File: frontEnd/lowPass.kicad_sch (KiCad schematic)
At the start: 15 parts, among them U201 BGS12P2L6E6327XTSA1, U202 BGS12P2L6E6327XTSA1

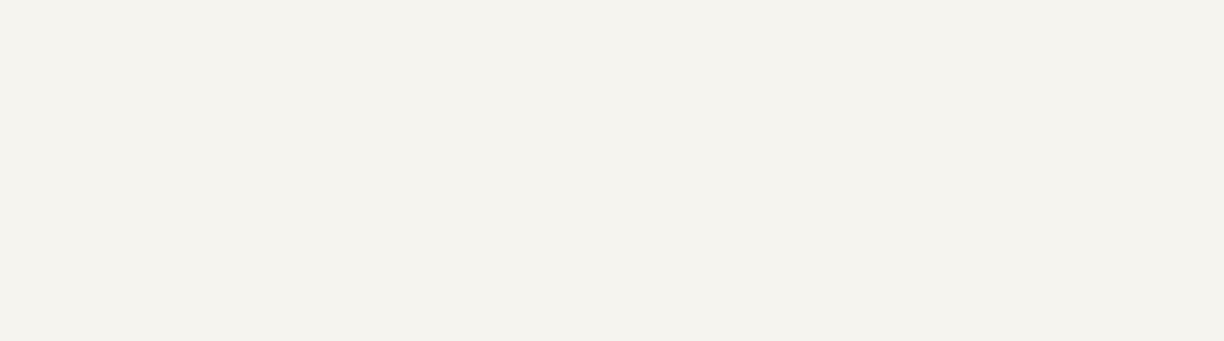
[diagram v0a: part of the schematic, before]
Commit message: update schematics, add bypass for the attenuator
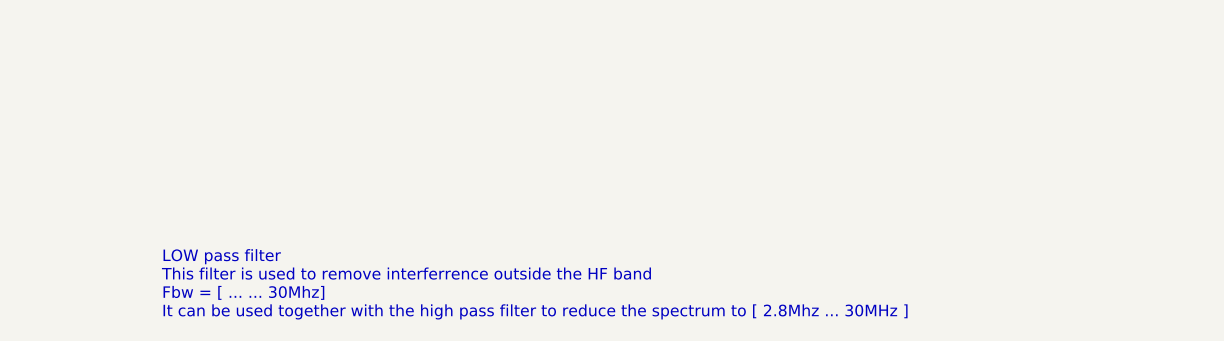
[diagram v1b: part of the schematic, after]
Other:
- note added: "LOW pass filter This filter is used to remove interferrence outside the HF band Fbw = [ ... ... 30Mhz] It can be used together with the high pass filter to reduce the spectrum to [ 2.8Mhz ... 30MHz ]"
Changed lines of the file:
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@@
     (stroke (width 0) (type default) (color 0 0 0 0))
+  )
+  (text "LOW pass filter\nThis filter is used to remove interferrence outside the HF band\nFbw = [ ... ... 30Mhz]\nIt can be used together with the high pass filter to reduce the spectrum to [ 2.8Mhz ... 30MHz ]"
+    (at 179.07 177.8 0)
+    (effects (font (size 1.27 1.27)) (justify left bottom))
   )
   (hierarchical_label "RF_IN" (shape input) (at 41.91 78.74 180)

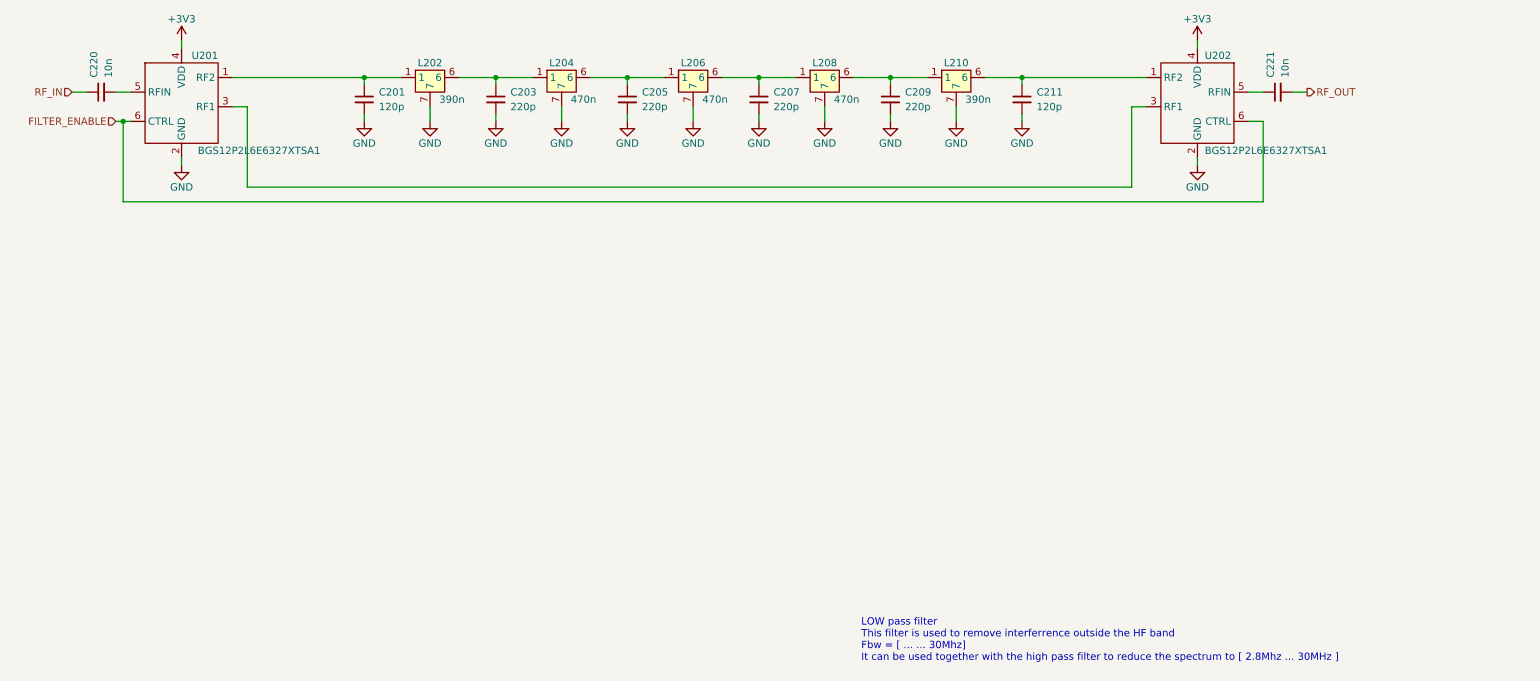
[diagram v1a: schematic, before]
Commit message: simply schematic: remove attenuator and gain blocks; add 5 way multiplexer
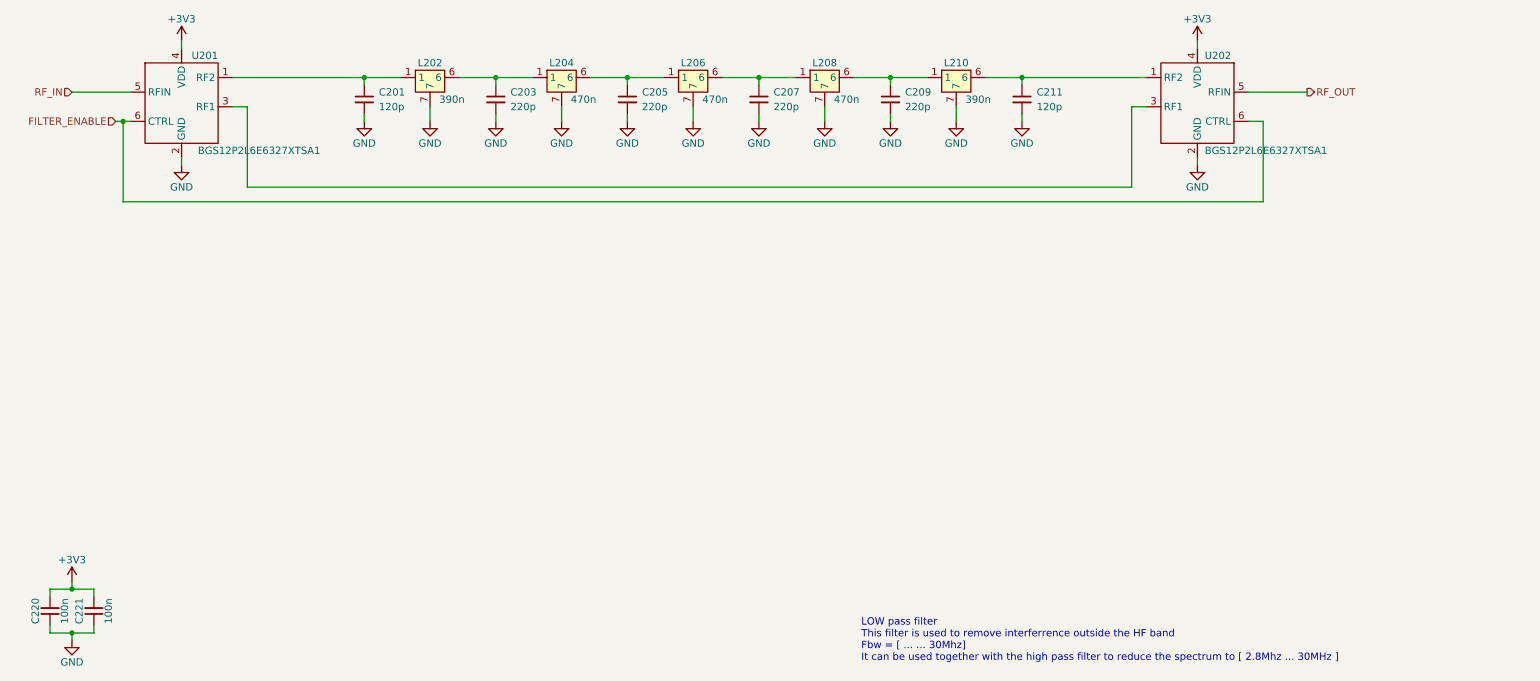
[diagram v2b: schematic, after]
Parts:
- C220, C221: value 10n -> 100n
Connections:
- net +3V3: now also C220.2, C221.2
- net GND: now also C220.1, C221.1
- net RF_IN: now also U201.5 (RFIN); no longer C220.1
- net RF_OUT: now also U202.5 (RFIN); no longer C221.2
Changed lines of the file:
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@@
   (junction (at 161.29 76.2) (diameter 0) (color 0 0 0 0)
   )
+  (junction (at 41.91 165.1) (diameter 0) (color 0 0 0 0)
+  )
   (junction (at 115.57 76.2) (diameter 0) (color 0 0 0 0)
   )
   (junction (at 207.01 76.2) (diameter 0) (color 0 0 0 0)
   )
+  (junction (at 41.91 172.72) (diameter 0) (color 0 0 0 0)
+  )
   (junction (at 184.15 76.2) (diameter 0) (color 0 0 0 0)
   )
@@
     (stroke (width 0) (type default) (color 0 0 0 0))
   )
+  (wire (pts (xy 41.91 172.72) (xy 41.91 173.99))
+    (stroke (width 0) (type default) (color 0 0 0 0))
+  )
   (wire (pts (xy 161.29 76.2) (xy 167.64 76.2))
     (stroke (width 0) (type default) (color 0 0 0 0))
@@
     (stroke (width 0) (type default) (color 0 0 0 0))
   )
+  (wire (pts (xy 41.91 172.72) (xy 45.72 172.72))
+    (stroke (width 0) (type default) (color 0 0 0 0))
+  )
   (wire (pts (xy 154.94 76.2) (xy 161.29 76.2))
     (stroke (width 0) (type default) (color 0 0 0 0))
@@
     (stroke (width 0) (type default) (color 0 0 0 0))
   )
-  (wire (pts (xy 41.91 78.74) (xy 44.45 78.74))
-    (stroke (width 0) (type default) (color 0 0 0 0))
-  )
   (wire (pts (xy 69.85 81.28) (xy 72.39 81.28))
     (stroke (width 0) (type default) (color 0 0 0 0))
@@
     (stroke (width 0) (type default) (color 0 0 0 0))
   )
-  (wire (pts (xy 254 78.74) (xy 256.54 78.74))
+  (wire (pts (xy 38.1 172.72) (xy 41.91 172.72))
     (stroke (width 0) (type default) (color 0 0 0 0))
   )
@@
     (stroke (width 0) (type default) (color 0 0 0 0))
   )
+  (wire (pts (xy 41.91 165.1) (xy 45.72 165.1))
+    (stroke (width 0) (type default) (color 0 0 0 0))
+  )
   (wire (pts (xy 127 81.28) (xy 127 83.82))
     (stroke (width 0) (type default) (color 0 0 0 0))
@@
     (stroke (width 0) (type default) (color 0 0 0 0))
   )
+  (wire (pts (xy 38.1 166.37) (xy 38.1 165.1))
+    (stroke (width 0) (type default) (color 0 0 0 0))
+  )
+  (wire (pts (xy 45.72 165.1) (xy 45.72 166.37))
+    (stroke (width 0) (type default) (color 0 0 0 0))
+  )
   (wire (pts (xy 226.06 81.28) (xy 226.06 95.25))
     (stroke (width 0) (type default) (color 0 0 0 0))
@@
     (stroke (width 0) (type default) (color 0 0 0 0))
   )
-  (wire (pts (xy 49.53 78.74) (xy 52.07 78.74))
+  (wire (pts (xy 38.1 165.1) (xy 41.91 165.1))
+    (stroke (width 0) (type default) (color 0 0 0 0))
+  )
+  (wire (pts (xy 38.1 171.45) (xy 38.1 172.72))
+    (stroke (width 0) (type default) (color 0 0 0 0))
+  )
+  (wire (pts (xy 41.91 78.74) (xy 52.07 78.74))
     (stroke (width 0) (type default) (color 0 0 0 0))
   )
@@
     (stroke (width 0) (type default) (color 0 0 0 0))
   )
+  (wire (pts (xy 45.72 171.45) (xy 45.72 172.72))
+    (stroke (width 0) (type default) (color 0 0 0 0))
+  )
   (wire (pts (xy 207.01 76.2) (xy 207.01 77.47))
     (stroke (width 0) (type default) (color 0 0 0 0))
@@
     (stroke (width 0) (type default) (color 0 0 0 0))
   )
-  (wire (pts (xy 246.38 78.74) (xy 248.92 78.74))
+  (wire (pts (xy 246.38 78.74) (xy 256.54 78.74))
+    (stroke (width 0) (type default) (color 0 0 0 0))
+  )
+  (wire (pts (xy 41.91 163.83) (xy 41.91 165.1))
     (stroke (width 0) (type default) (color 0 0 0 0))
   )
@@
     (effects (font (size 1.27 1.27)) (justify left))
   )
-  (symbol (lib_id "Device:C_Small") (at 46.99 78.74 90) (unit 1)
-    (in_bom yes) (on_board yes)
-    (property "Reference" "C220" (id 0) (at 45.7262 76.2 0)
-      (effects (font (size 1.27 1.27)) (justify left))
-    )
-    (property "Value" "10n" (id 1) (at 48.2662 76.2 0)
-      (effects (font (size 1.27 1.27)) (justify left))
-    )
-    (property "Footprint" "Capacitor_SMD:C_0805_2012Metric" (id 2) (at 46.99 78.74 0)
-      (effects (font (size 1.27 1.27)) hide)
-    )
-    (property "Datasheet" "~" (id 3) (at 46.99 78.74 0)
+  (symbol (lib_id "Device:C_Small") (at 45.72 168.91 180) (unit 1)
+    (in_bom yes) (on_board yes)
+    (property "Reference" "C221" (id 0) (at 43.18 168.91 90))
+    (property "Value" "100n" (id 1) (at 48.26 168.91 90))
+    (property "Footprint" "Capacitor_SMD:C_0805_2012Metric" (id 2) (at 45.72 168.91 0)
+      (effects (font (size 1.27 1.27)) hide)
+    )
+    (property "Datasheet" "~" (id 3) (at 45.72 168.91 0)
       (effects (font (size 1.27 1.27)) hide)
     )
@@
     (pin "2")
   )
-  (symbol (lib_id "Device:C_Small") (at 251.46 78.74 90) (unit 1)
-    (in_bom yes) (on_board yes)
-    (property "Reference" "C221" (id 0) (at 250.1962 76.2 0)
-      (effects (font (size 1.27 1.27)) (justify left))
-    )
-    (property "Value" "10n" (id 1) (at 252.7362 76.2 0)
-      (effects (font (size 1.27 1.27)) (justify left))
-    )
-    (property "Footprint" "Capacitor_SMD:C_0805_2012Metric" (id 2) (at 251.46 78.74 0)
-      (effects (font (size 1.27 1.27)) hide)
-    )
-    (property "Datasheet" "~" (id 3) (at 251.46 78.74 0)
+  (symbol (lib_id "power:+3V3") (at 41.91 163.83 0) (unit 1)
+    (in_bom yes) (on_board yes)
+    (property "Reference" "#PWR?" (id 0) (at 41.91 167.64 0)
+      (effects (font (size 1.27 1.27)) hide)
+    )
+    (property "Value" "+3V3" (id 1) (at 41.91 160.02 0))
+    (property "Footprint" "" (id 2) (at 41.91 163.83 0)
+      (effects (font (size 1.27 1.27)) hide)
+    )
+    (property "Datasheet" "" (id 3) (at 41.91 163.83 0)
+      (effects (font (size 1.27 1.27)) hide)
+    )
+    (pin "1")
+  )
+  (symbol (lib_id "Device:C_Small") (at 38.1 168.91 180) (unit 1)
+    (in_bom yes) (on_board yes)
+    (property "Reference" "C220" (id 0) (at 35.56 168.91 90))
+    (property "Value" "100n" (id 1) (at 40.64 168.91 90))
+    (property "Footprint" "Capacitor_SMD:C_0805_2012Metric" (id 2) (at 38.1 168.91 0)
+      (effects (font (size 1.27 1.27)) hide)
+    )
+    (property "Datasheet" "~" (id 3) (at 38.1 168.91 0)
       (effects (font (size 1.27 1.27)) hide)
     )
@@
     (pin "2")
   )
+  (symbol (lib_id "power:GND") (at 41.91 173.99 0) (unit 1)
+    (in_bom yes) (on_board yes)
+    (property "Reference" "#PWR?" (id 0) (at 41.91 180.34 0)
+      (effects (font (size 1.27 1.27)) hide)
+    )
+    (property "Value" "GND" (id 1) (at 41.91 177.8 0))
+    (property "Footprint" "" (id 2) (at 41.91 173.99 0)
+      (effects (font (size 1.27 1.27)) hide)
+    )
+    (property "Datasheet" "" (id 3) (at 41.91 173.99 0)
+      (effects (font (size 1.27 1.27)) hide)
+    )
+    (pin "1")
+  )
   (symbol (lib_id "Device:C_Small") (at 138.43 80.01 0) (unit 1)

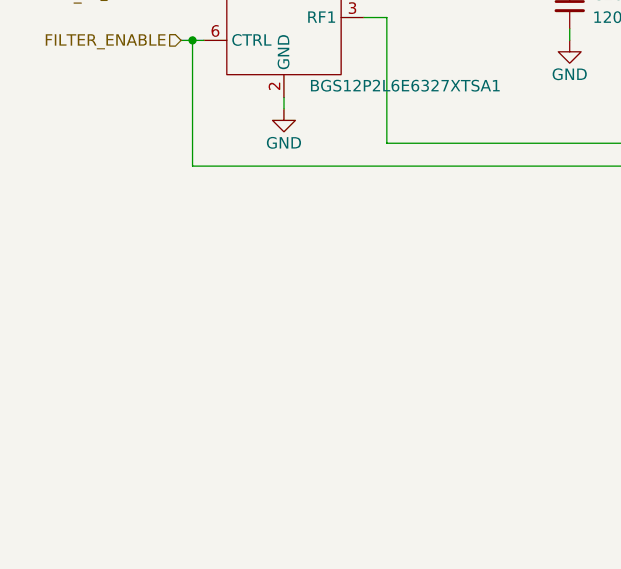
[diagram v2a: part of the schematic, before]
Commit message: add leds for each filter block
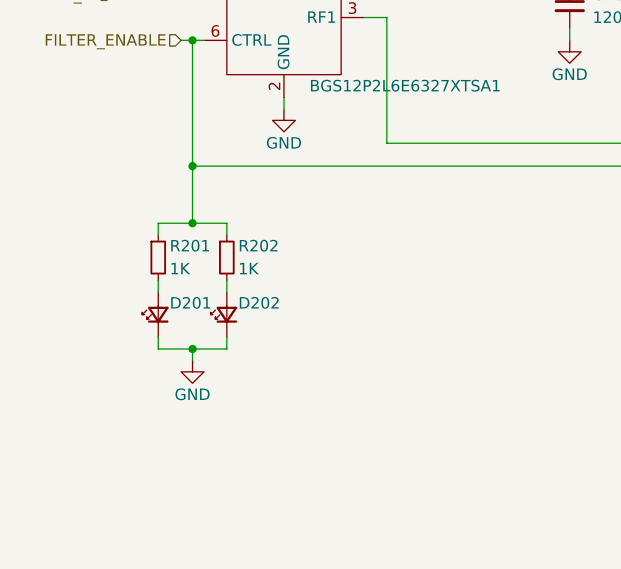
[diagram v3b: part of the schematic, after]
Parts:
- added D201, D202: LED_Small, LED_SMD:LED_0805_2012Metric, symbol Device:LED_Small
- added R201, R202: 1K, Resistor_SMD:R_0805_2012Metric, symbol Device:R_Small
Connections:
- net FILTER_ENABLE: now also R201.1, R202.1
- net GND: now also D201.1 (K), D202.1 (K)
- new net: D201.2 (A), R201.2
- new net: D202.2 (A), R202.2
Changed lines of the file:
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@@
   (junction (at 138.43 76.2) (diameter 0) (color 0 0 0 0)
   )
+  (junction (at 50.8 97.79) (diameter 0) (color 0 0 0 0)
+  )
+  (junction (at 50.8 118.11) (diameter 0) (color 0 0 0 0)
+  )
+  (junction (at 50.8 104.14) (diameter 0) (color 0 0 0 0)
+  )
   (junction (at 50.8 83.82) (diameter 0) (color 0 0 0 0)
   )
@@
     (stroke (width 0) (type default) (color 0 0 0 0))
   )
+  (wire (pts (xy 50.8 118.11) (xy 50.8 119.38))
+    (stroke (width 0) (type default) (color 0 0 0 0))
+  )
   (wire (pts (xy 154.94 76.2) (xy 161.29 76.2))
     (stroke (width 0) (type default) (color 0 0 0 0))
@@
     (stroke (width 0) (type default) (color 0 0 0 0))
   )
+  (wire (pts (xy 50.8 104.14) (xy 54.61 104.14))
+    (stroke (width 0) (type default) (color 0 0 0 0))
+  )
   (wire (pts (xy 69.85 81.28) (xy 72.39 81.28))
     (stroke (width 0) (type default) (color 0 0 0 0))
@@
     (stroke (width 0) (type default) (color 0 0 0 0))
   )
+  (wire (pts (xy 54.61 104.14) (xy 54.61 105.41))
+    (stroke (width 0) (type default) (color 0 0 0 0))
+  )
   (wire (pts (xy 138.43 76.2) (xy 144.78 76.2))
     (stroke (width 0) (type default) (color 0 0 0 0))
@@
     (stroke (width 0) (type default) (color 0 0 0 0))
   )
+  (wire (pts (xy 46.99 110.49) (xy 46.99 111.76))
+    (stroke (width 0) (type default) (color 0 0 0 0))
+  )
   (wire (pts (xy 184.15 82.55) (xy 184.15 83.82))
     (stroke (width 0) (type default) (color 0 0 0 0))
@@
     (stroke (width 0) (type default) (color 0 0 0 0))
   )
+  (wire (pts (xy 46.99 116.84) (xy 46.99 118.11))
+    (stroke (width 0) (type default) (color 0 0 0 0))
+  )
   (wire (pts (xy 226.06 81.28) (xy 226.06 95.25))
     (stroke (width 0) (type default) (color 0 0 0 0))
@@
     (stroke (width 0) (type default) (color 0 0 0 0))
   )
+  (wire (pts (xy 46.99 105.41) (xy 46.99 104.14))
+    (stroke (width 0) (type default) (color 0 0 0 0))
+  )
+  (wire (pts (xy 54.61 110.49) (xy 54.61 111.76))
+    (stroke (width 0) (type default) (color 0 0 0 0))
+  )
   (wire (pts (xy 38.1 171.45) (xy 38.1 172.72))
     (stroke (width 0) (type default) (color 0 0 0 0))
@@
     (stroke (width 0) (type default) (color 0 0 0 0))
   )
+  (wire (pts (xy 54.61 116.84) (xy 54.61 118.11))
+    (stroke (width 0) (type default) (color 0 0 0 0))
+  )
   (wire (pts (xy 60.96 69.85) (xy 60.96 71.12))
     (stroke (width 0) (type default) (color 0 0 0 0))
@@
     (stroke (width 0) (type default) (color 0 0 0 0))
   )
+  (wire (pts (xy 50.8 97.79) (xy 50.8 104.14))
+    (stroke (width 0) (type default) (color 0 0 0 0))
+  )
+  (wire (pts (xy 46.99 118.11) (xy 50.8 118.11))
+    (stroke (width 0) (type default) (color 0 0 0 0))
+  )
   (wire (pts (xy 207.01 76.2) (xy 207.01 77.47))
     (stroke (width 0) (type default) (color 0 0 0 0))
@@
   )
   (wire (pts (xy 60.96 90.17) (xy 60.96 91.44))
+    (stroke (width 0) (type default) (color 0 0 0 0))
+  )
+  (wire (pts (xy 46.99 104.14) (xy 50.8 104.14))
+    (stroke (width 0) (type default) (color 0 0 0 0))
+  )
+  (wire (pts (xy 50.8 118.11) (xy 54.61 118.11))
     (stroke (width 0) (type default) (color 0 0 0 0))
   )
@@
     (pin "1")
   )
+  (symbol (lib_id "power:GND") (at 50.8 119.38 0) (unit 1)
+    (in_bom yes) (on_board yes)
+    (property "Reference" "#PWR?" (id 0) (at 50.8 125.73 0)
+      (effects (font (size 1.27 1.27)) hide)
+    )
+    (property "Value" "GND" (id 1) (at 50.8 123.19 0))
+    (property "Footprint" "" (id 2) (at 50.8 119.38 0)
+      (effects (font (size 1.27 1.27)) hide)
+    )
+    (property "Datasheet" "" (id 3) (at 50.8 119.38 0)
+      (effects (font (size 1.27 1.27)) hide)
+    )
+    (pin "1")
+  )
   (symbol (lib_id "Device:C_Small") (at 184.15 80.01 0) (unit 1)
     (in_bom yes) (on_board yes)
@@
     )
     (property "Datasheet" "~" (id 3) (at 184.15 80.01 0)
+      (effects (font (size 1.27 1.27)) hide)
+    )
+    (pin "1")
+    (pin "2")
+  )
+  (symbol (lib_id "Device:R_Small") (at 46.99 107.95 0) (unit 1)
+    (in_bom yes) (on_board yes)
+    (property "Reference" "R201" (id 0) (at 48.26 106.68 0)
+      (effects (font (size 1.27 1.27)) (justify left))
+    )
+    (property "Value" "1K" (id 1) (at 48.26 109.22 0)
+      (effects (font (size 1.27 1.27)) (justify left))
+    )
+    (property "Footprint" "Resistor_SMD:R_0805_2012Metric" (id 2) (at 46.99 107.95 0)
+      (effects (font (size 1.27 1.27)) hide)
+    )
+    (property "Datasheet" "~" (id 3) (at 46.99 107.95 0)
       (effects (font (size 1.27 1.27)) hide)
     )
@@
     (pin "1")
   )
+  (symbol (lib_id "Device:LED_Small") (at 54.61 114.3 90) (unit 1)
+    (in_bom yes) (on_board yes)
+    (property "Reference" "D202" (id 0) (at 55.88 113.03 90)
+      (effects (font (size 1.27 1.27)) (justify right))
+    )
+    (property "Value" "LED_Small" (id 1) (at 57.15 115.5064 90)
+      (effects (font (size 1.27 1.27)) (justify right) hide)
+    )
+    (property "Footprint" "LED_SMD:LED_0805_2012Metric" (id 2) (at 54.61 114.3 90)
+      (effects (font (size 1.27 1.27)) hide)
+    )
+    (property "Datasheet" "~" (id 3) (at 54.61 114.3 90)
+      (effects (font (size 1.27 1.27)) hide)
+    )
+    (pin "1")
+    (pin "2")
+  )
   (symbol (lib_id "frontEnd:TOKO_10K_SERIES") (at 193.04 76.2 0) (unit 1)
     (in_bom yes) (on_board yes)
@@
     (pin "2")
   )
+  (symbol (lib_id "Device:LED_Small") (at 46.99 114.3 90) (unit 1)
+    (in_bom yes) (on_board yes)
+    (property "Reference" "D201" (id 0) (at 48.26 113.03 90)
+      (effects (font (size 1.27 1.27)) (justify right))
+    )
+    (property "Value" "LED_Small" (id 1) (at 49.53 115.5064 90)
+      (effects (font (size 1.27 1.27)) (justify right) hide)
+    )
+    (property "Footprint" "LED_SMD:LED_0805_2012Metric" (id 2) (at 46.99 114.3 90)
+      (effects (font (size 1.27 1.27)) hide)
+    )
+    (property "Datasheet" "~" (id 3) (at 46.99 114.3 90)
+      (effects (font (size 1.27 1.27)) hide)
+    )
+    (pin "1")
+    (pin "2")
+  )
   (symbol (lib_id "power:GND") (at 237.49 91.44 0) (unit 1)
     (in_bom yes) (on_board yes)
@@
     (pin "1")
   )
+  (symbol (lib_id "Device:R_Small") (at 54.61 107.95 0) (unit 1)
+    (in_bom yes) (on_board yes)
+    (property "Reference" "R202" (id 0) (at 55.88 106.68 0)
+      (effects (font (size 1.27 1.27)) (justify left))
+    )
+    (property "Value" "1K" (id 1) (at 55.88 109.22 0)
+      (effects (font (size 1.27 1.27)) (justify left))
+    )
+    (property "Footprint" "Resistor_SMD:R_0805_2012Metric" (id 2) (at 54.61 107.95 0)
+      (effects (font (size 1.27 1.27)) hide)
+    )
+    (property "Datasheet" "~" (id 3) (at 54.61 107.95 0)
+      (effects (font (size 1.27 1.27)) hide)
+    )
+    (pin "1")
+    (pin "2")
+  )
   (symbol (lib_id "power:GND") (at 115.57 83.82 0) (unit 1)
